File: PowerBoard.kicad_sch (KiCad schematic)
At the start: 136 parts, among them IC1 LT1910ES8#PBF, IC2 LT1910ES8#PBF, IC3 LT1910ES8#PBF, IC4 LT1910ES8#PBF, IC5 LT1910ES8#PBF, IC7 MAX17541GATB+T, J1 XT90, J10 XT90, J11 XT90, J12 XT90, J13 XT90, J14 DEAN_T, J15 DEAN_T, J16 DEAN_T, J17 DEAN_T, J18 DEAN_T, J19 DEAN_T, J2 DEAN_T, J20 XT60, J21 XT60, J22 XT60, J23 XT60, J24 XT60, J25 XT60, J26 XT60, J27 XT60, J28 XT60, J29 XT60, J3 XT60, J30 XT60, J31 XT60, J32 XT30, J33 XT30, J34 XT30, J35 XT30, J36 XT30, J37 XT30, J38 XT30, J39 XT30, J4 XT30, J40 XT30, J41 XT60, J5 Conn_01x02, J6 XT90, J7 XT90, J8 XT90, J9 XT90, Q1 IRFS7530TRL7PP, Q2 IRFS7437TRLPBF, Q3 IRFS7437TRLPBF, Q4 IRFS7437TRLPBF, Q5 IRFS7437TRLPBF, U1 Pico, U2 INA238, U3 INA238, U4 INA238, U5 INA238, U6 INA238

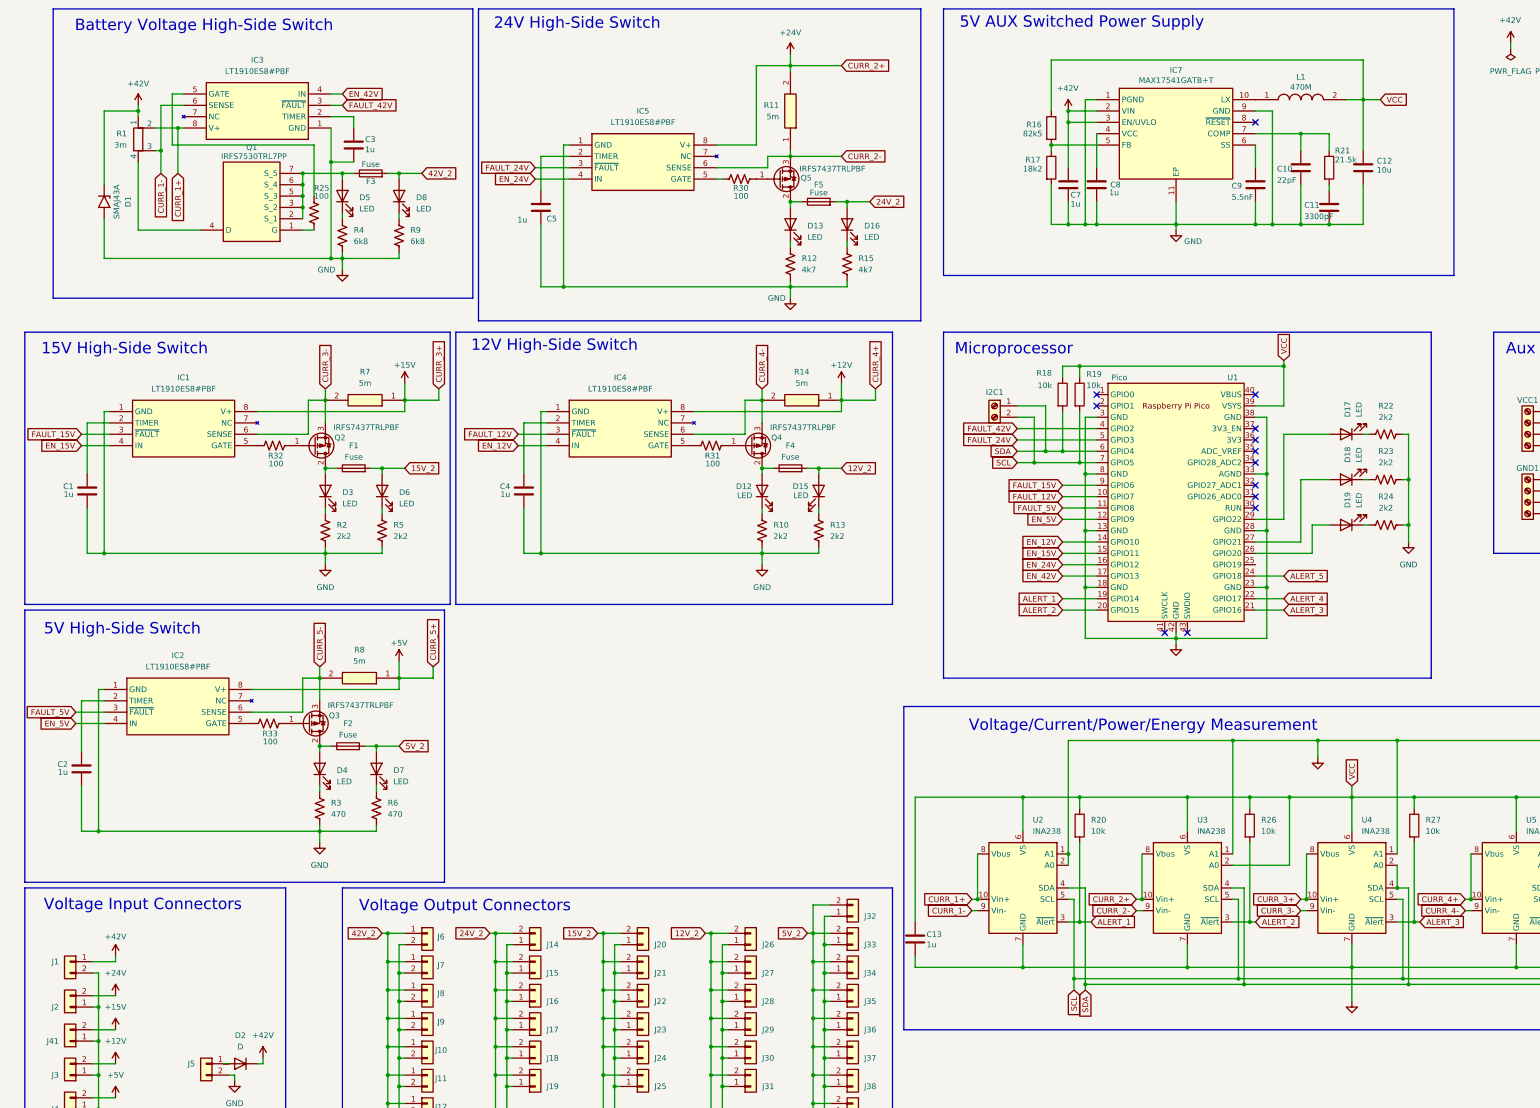
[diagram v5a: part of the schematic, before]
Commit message: safety features added, uart connector added
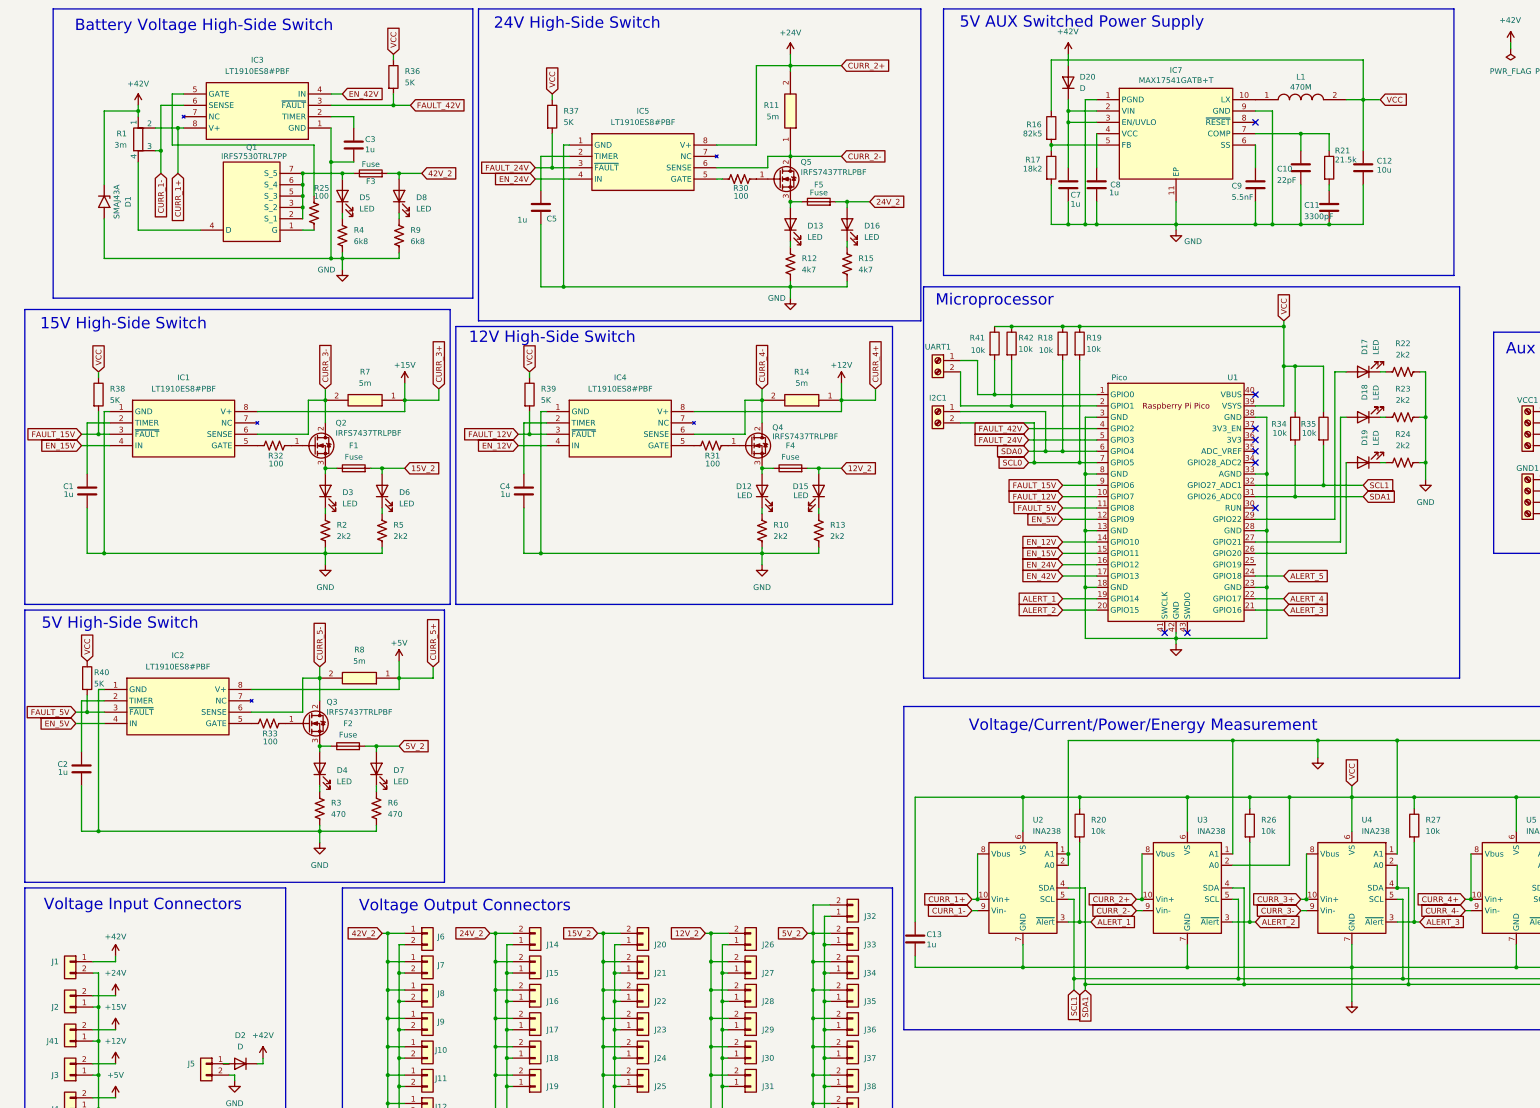
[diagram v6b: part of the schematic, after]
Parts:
- added D20: D, Diode_SMD:D_1206_3216Metric, symbol Device:D
- added R34, R35, R41, R42: 10k, Resistor_SMD:R_1206_3216Metric, symbol Device:R
- added R36, R37, R38, R39, R40: 5K, Resistor_SMD:R_1206_3216Metric, symbol Device:R
- added UART1: Screw_Terminal_01x02, TerminalBlock:TerminalBlock_Xinya_XY308-2.54-2P_1x02_P2.54mm_Horizontal, symbol Connector:Screw_Terminal_01x02
- Q2, Q3, Q4, Q5: symbol Transistor_FET:IRF9540N -> Transistor_FET:BUK7880-55A
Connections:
- net +42V: now also D20.2 (A); no longer C7.1, IC7.2 (VIN), IC7.3 (EN/UVLO)
- net CURR_2-: now also Q5.2 (D); no longer Q5.3 (S)
- net CURR_3-: now also Q2.2 (D); no longer Q2.3 (S)
- net CURR_4-: now also Q4.2 (D); no longer Q4.3 (S)
- net CURR_5-: now also Q3.2 (D); no longer Q3.3 (S)
- net FAULT_12V: now also R39.2
- net FAULT_15V: now also R38.2
- net FAULT_24V: now also R37.2
- net FAULT_42V: now also R36.2
- net FAULT_5V: now also R40.2
- net VCC: now also R34.1, R35.1, R36.1, R37.1, R38.1, R39.1, R40.1, R41.1, R42.1
- net at D12.2 (A), F4.1: now also Q4.3 (S); no longer Q4.2 (D)
- net at D13.2 (A), F5.1: now also Q5.3 (S); no longer Q5.2 (D)
- net at D4.2 (A), F2.1: now also Q3.3 (S); no longer Q3.2 (D)
- net at U1.1 (GPIO0): now also R41.2, UART1.1 (Pin_1)
- net at U1.2 (GPIO1): now also R42.2, UART1.2 (Pin_2)
- net SDA1: now reaches U1.31 (GPIO26_ADC0)
- net SDA1: now also U2.4 (SDA), U3.4 (SDA), U4.2 (A0), U4.4 (SDA), U5.4 (SDA), U6.4 (SDA), R34.2
- net SCL1: now reaches U1.32 (GPIO27_ADC1)
- net SCL1: now also U2.5 (SCL), U3.5 (SCL), U4.5 (SCL), U5.2 (A0), U5.5 (SCL), U6.5 (SCL), R35.2
- net at D3.2 (A), F1.1: now also Q2.3 (S); no longer Q2.2 (D)
- removed net SCL: I2C1.2 (Pin_2), R19.2, U1.7 (GPIO5), U2.5 (SCL), U3.5 (SCL), U4.5 (SCL), U5.2 (A0), U5.5 (SCL), U6.5 (SCL)
- removed net SDA: I2C1.1 (Pin_1), R18.2, U1.6 (GPIO4), U2.4 (SDA), U3.4 (SDA), U4.2 (A0), U4.4 (SDA), U5.4 (SDA), U6.4 (SDA)
- new net: C7.1, D20.1 (K), IC7.2 (VIN), IC7.3 (EN/UVLO)
- new net SCL0: I2C1.2 (Pin_2), R19.2, U1.7 (GPIO5)
- new net SDA0: I2C1.1 (Pin_1), R18.2, U1.6 (GPIO4)
- no-connect marks 13 -> 9
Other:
- moved on the sheet: D17, D18, D19, I2C1, R18, R19, R22, R23, R24
